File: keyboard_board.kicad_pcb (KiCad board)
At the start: 2 copper layers, 85.1 x 51 mm, 16 parts, among them J1 Conn_02x20_Odd_Even, J2 Trackpad Connector, J3 Rp500KB, J4 USB_C_Receptacle_USB2.0_16P, P1 S2B-PH-SM4-TB, P2 S2B-PH-SM4-TB, U1 SC0915, U2 74HC165, U3 74HC165, U4 LM66100DCK

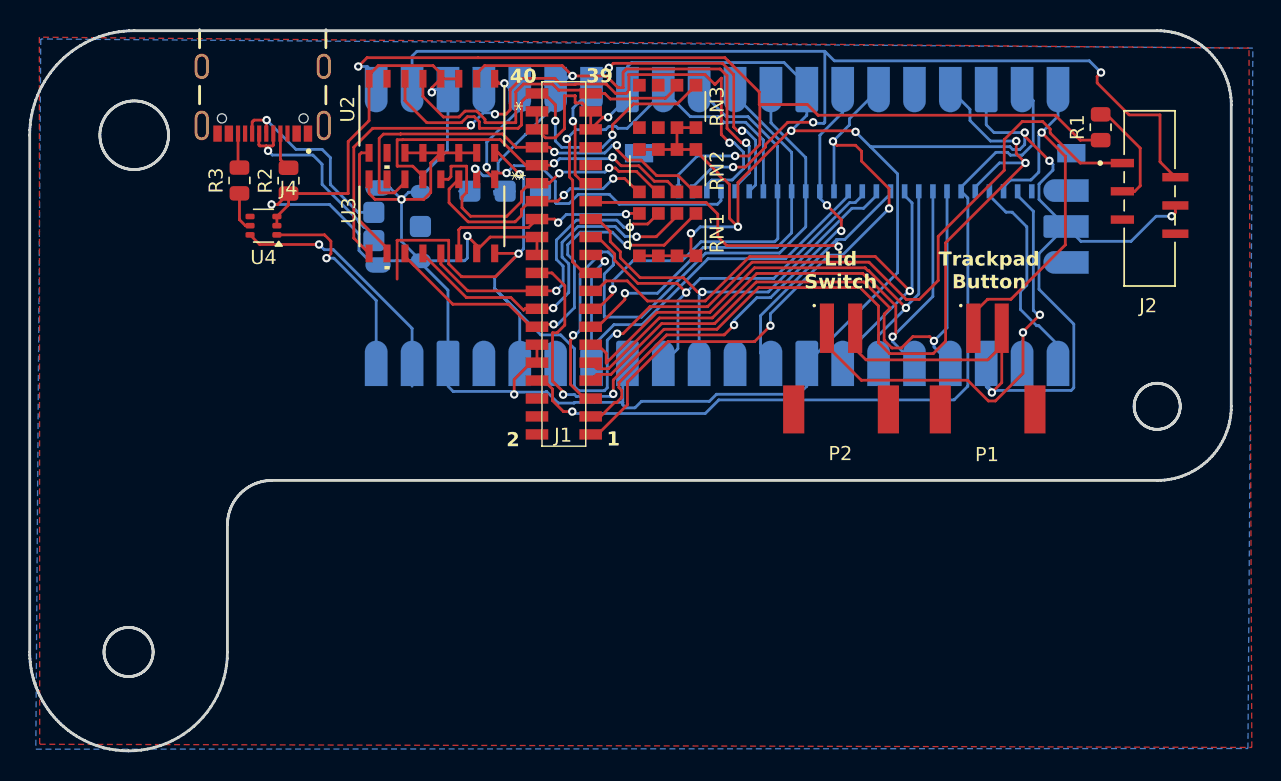
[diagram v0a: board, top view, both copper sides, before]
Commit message: -Changes USB labels to support differential pair - Does some major layout changes.
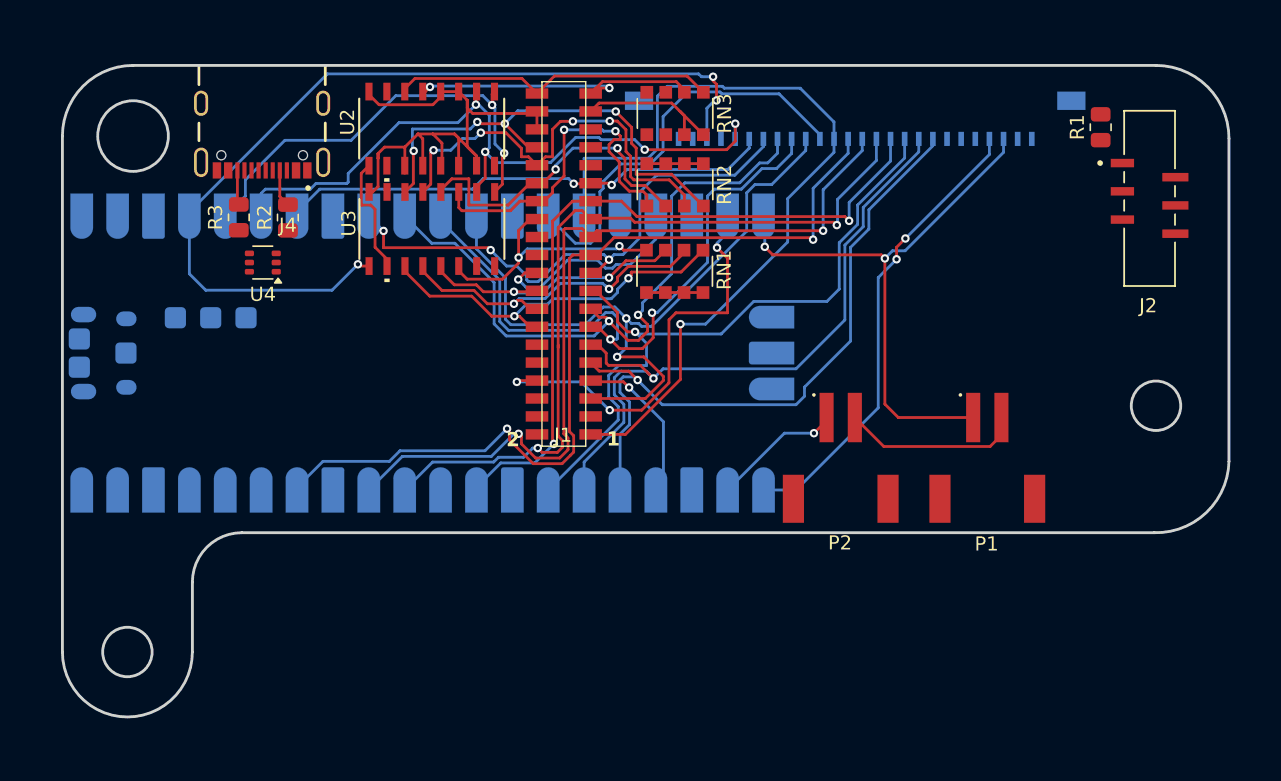
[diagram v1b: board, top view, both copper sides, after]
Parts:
- moved U1 22.7 mm to (205.5, 95.9)
- moved P1 6.32 mm to (245.5, 100.4)
- moved P2 6.32 mm to (235.1, 100.4)
- moved J3 3.71 mm to (236.2, 79.8)
- moved RN1 2.65 mm to (223.4, 90.1)
- moved J4 2.61 mm to (194.2, 78.2)
- moved U4 2.61 mm to (194.2, 89.5)
- moved R2 2.61 mm to (196.0, 86.3)
- moved R3 2.61 mm to (192.5, 86.3)
- moved RN2 1.13 mm to (223.4, 84.0)
- moved U2 0.91 mm to (206.2, 80.0)
- moved U3 0.90 mm to (206.2, 87.1)
- moved RN3 0.73 mm to (223.4, 78.9)
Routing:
- net GND: track 299.7 -> 73.6 mm, vias 14 -> 0
- net +3.3V: track 99.4 -> 0.00 mm, vias 3 -> 0
- net TP_RX: track 79.8 -> 0.00 mm, vias 3 -> 0
- net TP_TX: track 67.8 -> 0.00 mm, vias 2 -> 0
- net Power LED V+: track 73.8 -> 15.0 mm, vias 4 -> 1
- net Row 7: track 44.6 -> 11.4 mm
- net Row 23: track 29.9 -> 60.7 mm, vias 1 -> 2
- net Row 21: track 33.3 -> 63.6 mm, vias 1 -> 2
- net Caps LED V+: track 57.7 -> 30.2 mm, vias 1 -> 3
- net Row 25: track 31.3 -> 56.8 mm, vias 1 -> 2
- net LidSwitch: track 33.9 -> 9.25 mm, vias 2 -> 1
- net VSYS: track 18.3 -> 0.00 mm, vias 1 -> 0
- net RGB: track 14.9 -> 33.1 mm, vias 0 -> 2
- net Meta 13 (Ctrl): track 29.7 -> 46.5 mm, vias 1 -> 2
- net Meta 15 (L Shift): track 29.7 -> 46.3 mm, vias 1 -> 2
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- removed copper zone on F.Cu, net +3.3V
- removed copper zone on B.Cu, net GND
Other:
- board size 85.1 x 51 mm -> 82.6 x 46.1 mm
- board text removed: "39"
- board text removed: "40"
- board text removed: "Lid Switch"
- board text removed: "Trackpad Button"

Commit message: Adds Power input 2-pin JST PH. Adds RGB output Adds Power Button input
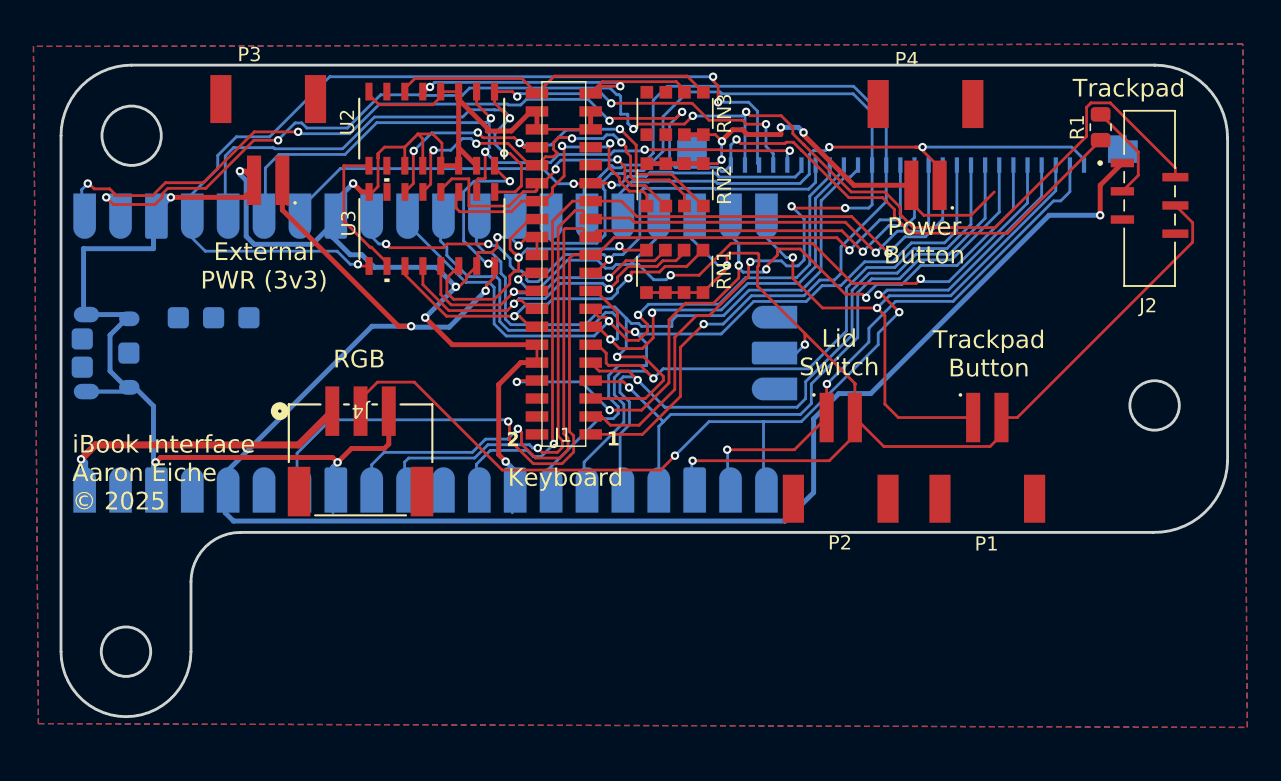
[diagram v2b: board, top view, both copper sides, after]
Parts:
- removed R2, R3: 5.1k, Resistor_SMD:R_0805_2012Metric
- removed U4: LM66100DCK, Package_TO_SOT_SMD:SOT-363_SC-70-6
- added P3: S2B-PH-SM4-TB, Aaron:JST_S2B-PH-SM4-TB, F.Cu at (194.6, 83.6)
- added P4: S2B-PH-SM4-TB, Aaron:JST_S2B-PH-SM4-TB, F.Cu at (241.1, 84.0)
- J3: footprint Connector_FFC-FPC:Molex_200528-0260_1x26-1MP_P1.00mm_Horizontal -> Aaron:AMPHENOL_F52R-1A7H1-11026
- J4: value USB_C_Receptacle_USB2.0_16P -> S3B-PH-SM4-TB; footprint Aaron:GCT_USB4105-GF-A -> Aaron:CONN3_S3B-PH_JST
- moved J4 26.2 mm to (201.1, 103.4)
- moved J3 3.70 mm to (239.8, 79.8)
- moved U1 0.21 mm to (205.7, 95.9)
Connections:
- J3 pad 26: unconnected-(J3-GP29-Pad26) -> PowerSwitch
- U1 pad 16: unconnected-(U1-GP12-Pad16) -> PowerSwitch
- U1 pad TP2: USB_DM -> unconnected-(U1-TP2_USB_DM-PadTP2)
- U1 pad TP3: USB_DP -> unconnected-(U1-TP3_USB_DP-PadTP3)
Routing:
- net GND: track 73.6 -> 297.1 mm, vias 0 -> 17
- net +3.3V: track 0.00 -> 136.3 mm, vias 0 -> 5
- net TP_RX: track 0.00 -> 99.5 mm, vias 0 -> 5
- net TP_TX: track 0.00 -> 91.2 mm, vias 0 -> 5
- net Meta 3 (Option): track 29.4 -> 73.5 mm, vias 0 -> 3
- net PowerSwitch: track 0.00 -> 41.1 mm, vias 0 -> 2
- net RGB: track 33.1 -> 70.7 mm, vias 2 -> 3
- net Power LED V+: track 15.0 -> 51.0 mm, vias 1 -> 3
- net Row 7: track 11.4 -> 47.3 mm
- net LidSwitch: track 9.25 -> 38.5 mm, vias 1 -> 2
- net Paralell Latch: track 31.2 -> 60.4 mm, vias 2 -> 5
- net Caps LED V+: track 30.2 -> 58.9 mm, vias 3 -> 5
- net VBUS: track 0.00 -> 21.5 mm, vias 0 -> 1
- net Meta 1 (Fn): track 59.7 -> 67.5 mm
- net Net-(J2-Pin_3): track 0.00 -> 7.02 mm
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- added copper zone on B.Cu, net +3.3V
- added copper zone on F.Cu, net GND
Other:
- outline, holes or cut-outs redrawn
- board text added: "External PWR (3v3)"
- board text added: "Keyboard"
- board text added: "Lid Switch"
- board text added: "Power Button"
- board text added: "RGB"
- board text added: "Trackpad"
- board text added: "Trackpad Button"
- board text added: "iBook Interface Aaron Eiche © 2025"
- board text removed: "${REFERENCE}"
